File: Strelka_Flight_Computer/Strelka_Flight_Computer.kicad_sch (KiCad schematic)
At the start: 10 parts

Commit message: Started design for V2
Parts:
- removed R14, R15, R16, R17, R18, R19: 0, Resistor_SMD:R_0603_1608Metric_Pad0.98x0.95mm_HandSolder, symbol Device:R_Small
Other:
- removed sheet STM32F405
- added sheet STM32F407 (STM32F407.kicad_sch)
- sheet Actuators ports: added none; removed CONT_TEST_EN
- sheet Data_Interfaces ports: added CAN_RXD, CAN_TXD; removed SWCLK, SWDIO

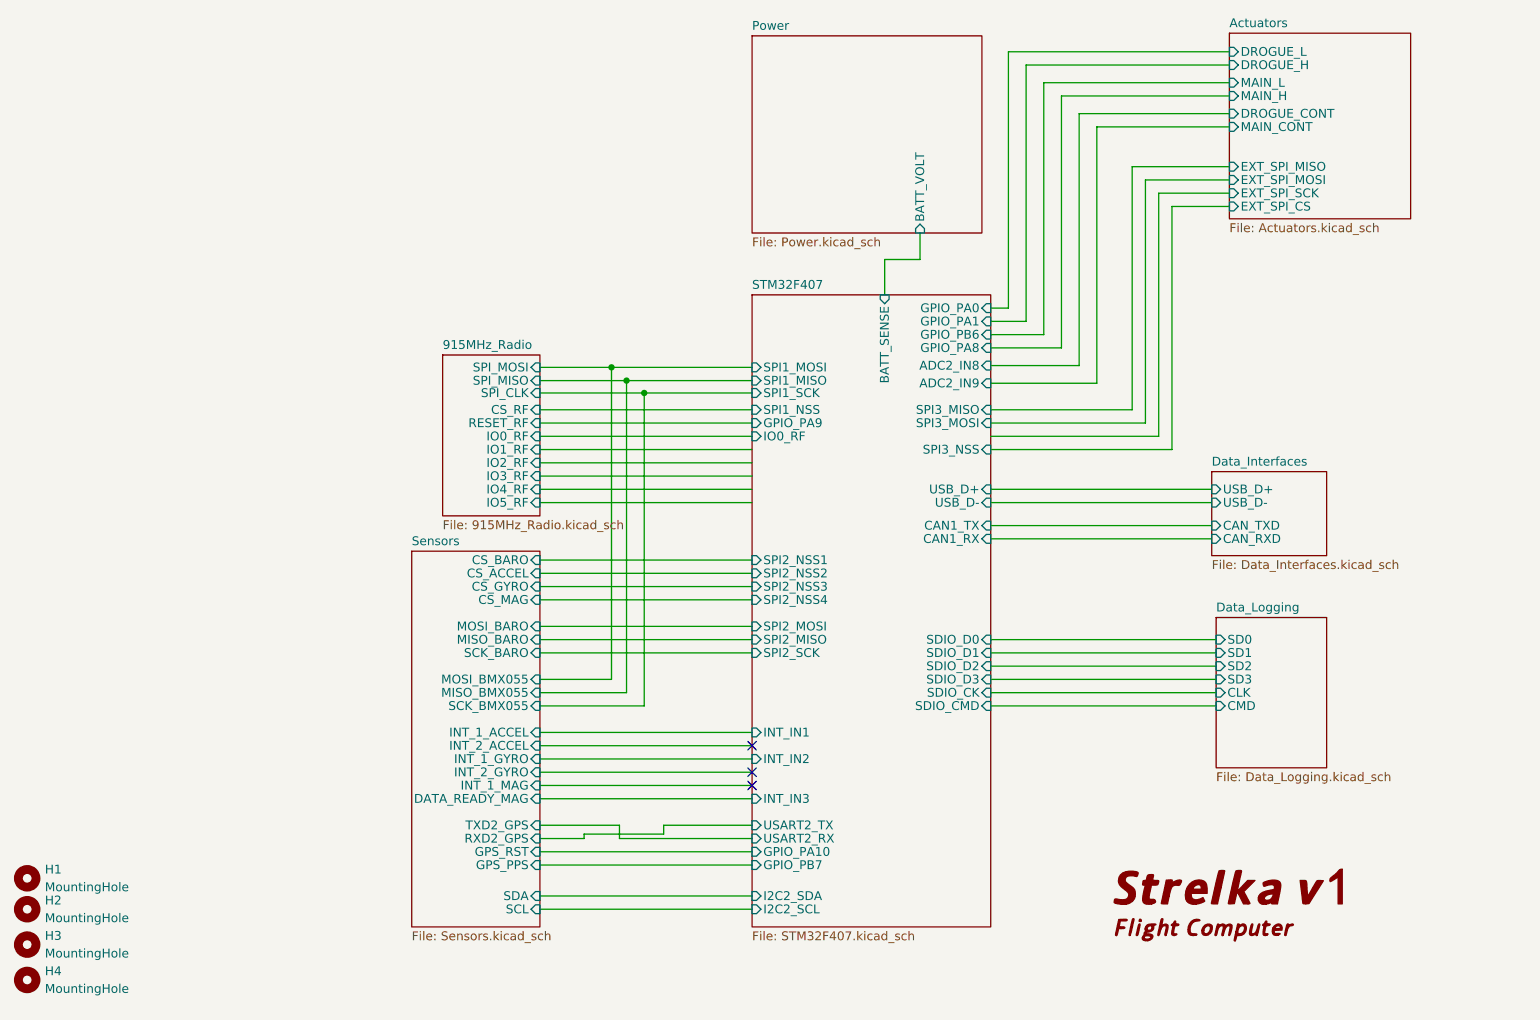
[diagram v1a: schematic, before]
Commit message: Changes main processor to h4745
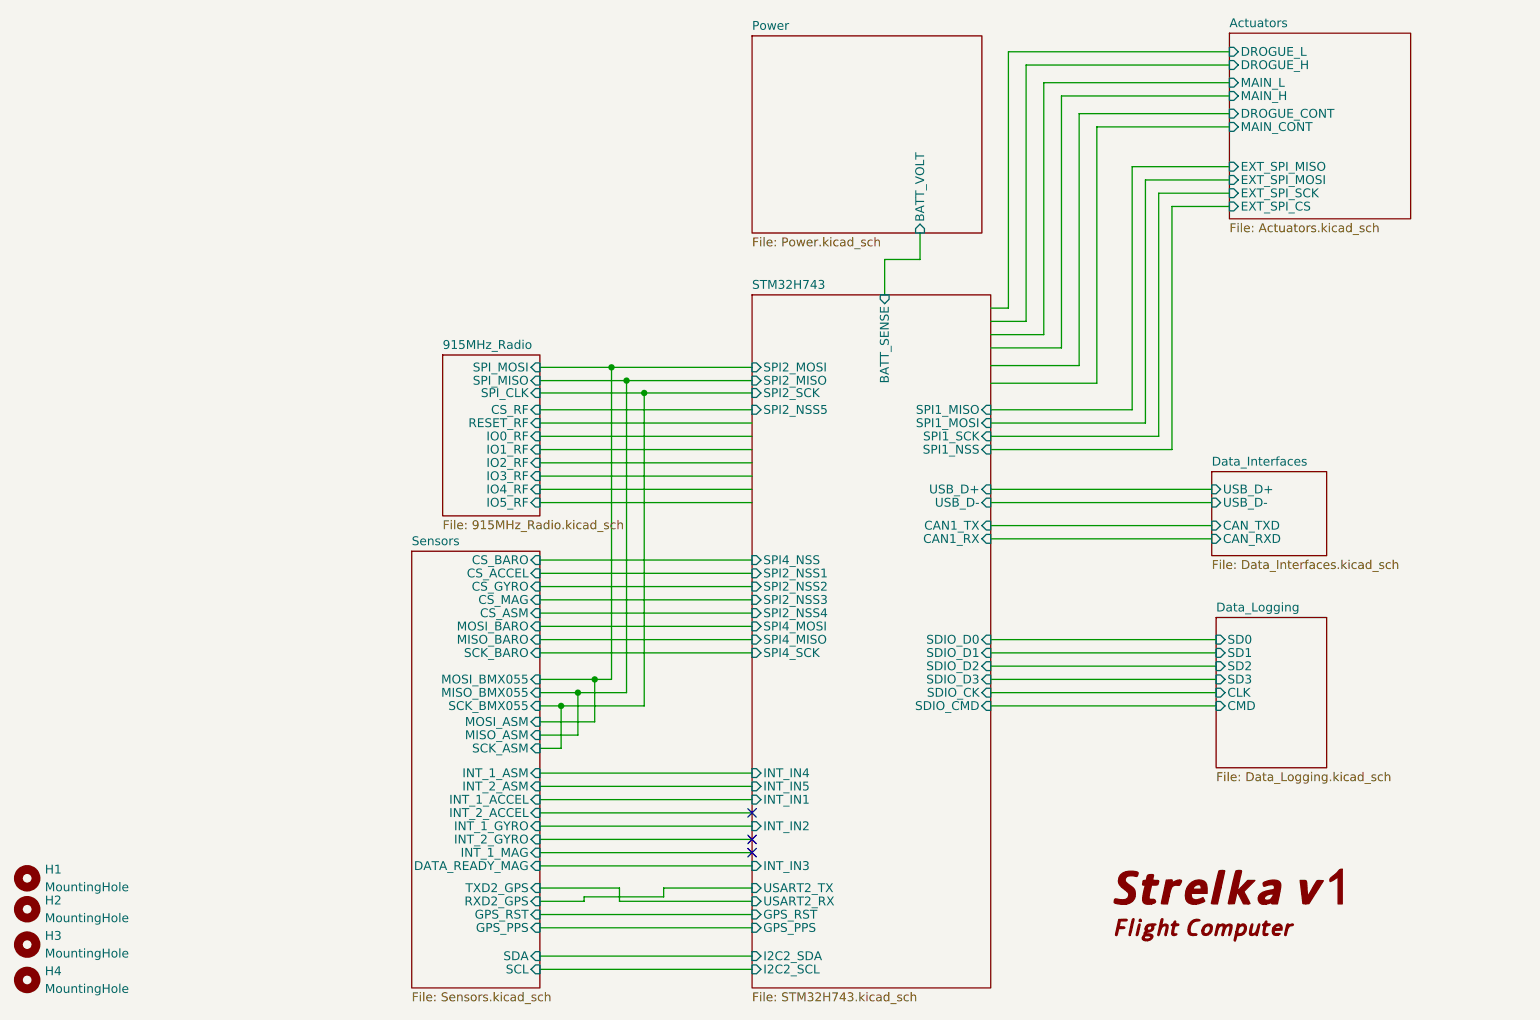
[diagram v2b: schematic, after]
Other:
- removed sheet STM32F407
- added sheet STM32H743 (STM32H743.kicad_sch)
- sheet Sensors ports: added CS_ASM, INT_1_ASM, INT_2_ASM, MISO_ASM, MOSI_ASM, SCK_ASM; removed none

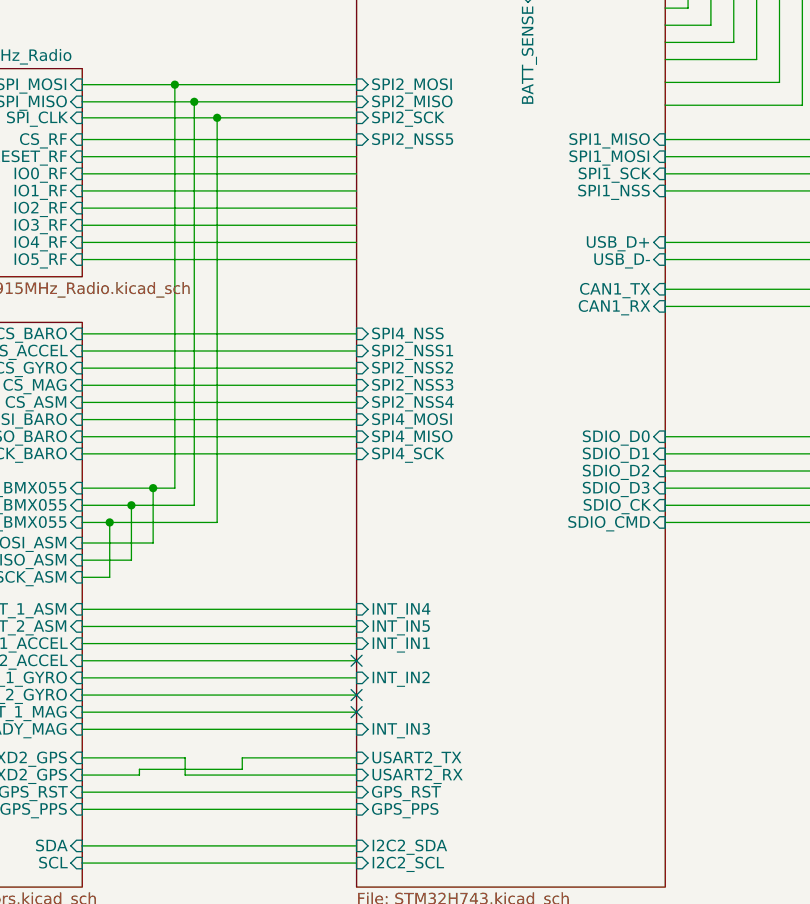
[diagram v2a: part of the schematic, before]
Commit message: Started component placement
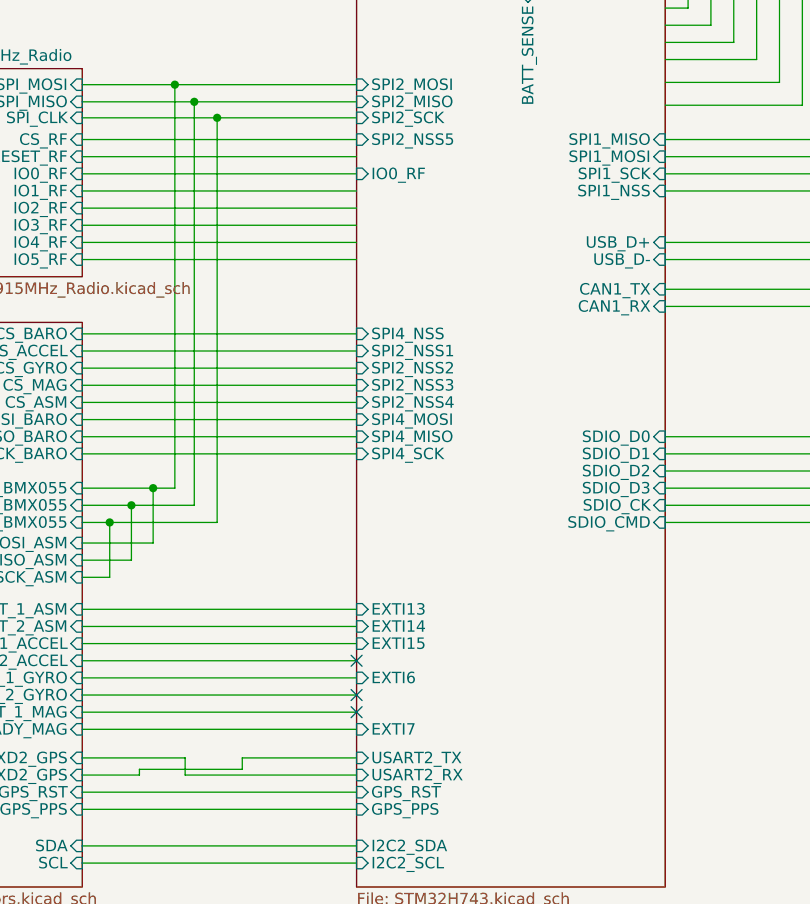
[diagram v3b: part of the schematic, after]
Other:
- sheet STM32H743 ports: added EXTI13, EXTI14, EXTI15, EXTI6, EXTI7, IO0_RF; removed INT_IN1, INT_IN2, INT_IN3, INT_IN4, INT_IN5
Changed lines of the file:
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@@
       (effects (font (size 1.27 1.27)) (justify right))
-    )
-    (pin "INT_IN1" input (at 127 158.877 180)
-      (effects (font (size 1.27 1.27)) (justify left))
     )
     (pin "SPI2_MISO" input (at 127 98.679 180)
@@
     (pin "SDIO_D1" input (at 161.29 137.795 0)
       (effects (font (size 1.27 1.27)) (justify right))
-    )
-    (pin "INT_IN3" input (at 127 168.402 180)
-      (effects (font (size 1.27 1.27)) (justify left))
-    )
-    (pin "INT_IN2" input (at 127 162.687 180)
-      (effects (font (size 1.27 1.27)) (justify left))
     )
     (pin "I2C2_SCL" input (at 127 183.261 180)
@@
       (effects (font (size 1.27 1.27)) (justify left))
     )
-    (pin "INT_IN4" input (at 127 155.067 180)
-      (effects (font (size 1.27 1.27)) (justify left))
-    )
-    (pin "INT_IN5" input (at 127 156.972 180)
-      (effects (font (size 1.27 1.27)) (justify left))
-    )
     (pin "GPS_PPS" input (at 127 177.292 180)
       (effects (font (size 1.27 1.27)) (justify left))
@@
       (effects (font (size 1.27 1.27)) (justify left))
     )
+    (pin "EXTI13" input (at 127 155.067 180)
+      (effects (font (size 1.27 1.27)) (justify left))
+    )
+    (pin "EXTI14" input (at 127 156.972 180)
+      (effects (font (size 1.27 1.27)) (justify left))
+    )
+    (pin "EXTI15" input (at 127 158.877 180)
+      (effects (font (size 1.27 1.27)) (justify left))
+    )
+    (pin "EXTI6" input (at 127 162.687 180)
+      (effects (font (size 1.27 1.27)) (justify left))
+    )
+    (pin "EXTI7" input (at 127 168.402 180)
+      (effects (font (size 1.27 1.27)) (justify left))
+    )
+    (pin "IO0_RF" input (at 127 106.68 180)
+      (effects (font (size 1.27 1.27)) (justify left))
+    )

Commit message: Routing complete
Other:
- sheet STM32H743 ports: added DROGUE_H, DROGUE_L, MAIN_H, MAIN_L; removed none
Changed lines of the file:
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@@
       (effects (font (size 1.27 1.27)) (justify left))
+    )
+    (pin "MAIN_L" input (at 161.29 92.075 0)
+      (effects (font (size 1.27 1.27)) (justify right))
+    )
+    (pin "MAIN_H" input (at 161.29 93.98 0)
+      (effects (font (size 1.27 1.27)) (justify right))
+    )
+    (pin "DROGUE_L" input (at 161.29 88.265 0)
+      (effects (font (size 1.27 1.27)) (justify right))
+    )
+    (pin "DROGUE_H" input (at 161.29 90.17 0)
+      (effects (font (size 1.27 1.27)) (justify right))
     )
     (instances

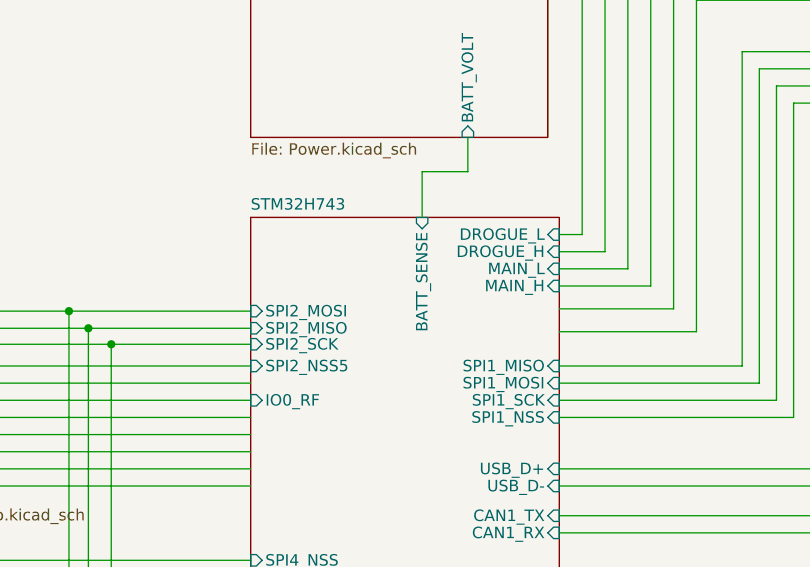
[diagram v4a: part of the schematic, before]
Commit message: Created BOM
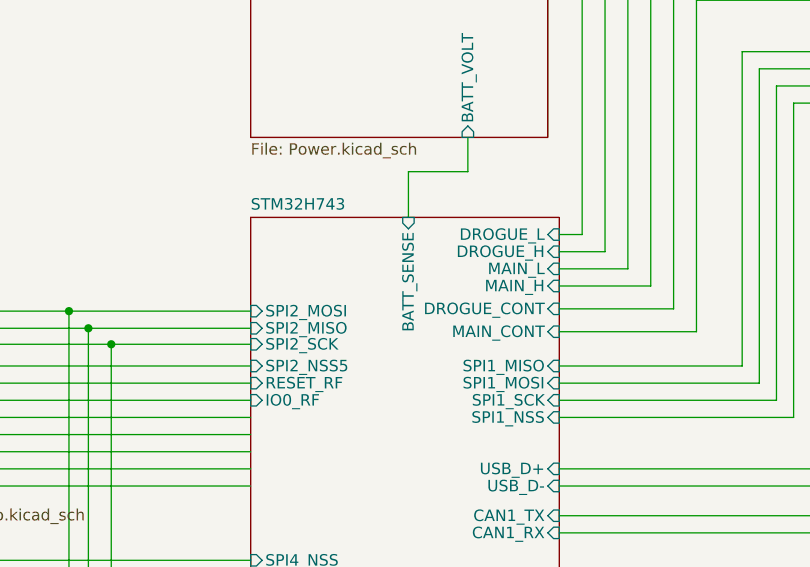
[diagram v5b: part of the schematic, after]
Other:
- sheet STM32H743 ports: added DROGUE_CONT, MAIN_CONT, RESET_RF; removed none
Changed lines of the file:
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@@
     (stroke (width 0) (type default))
   )
-  (wire (pts (xy 146.05 86.36) (xy 146.05 81.28))
+  (wire (pts (xy 144.526 86.36) (xy 144.526 81.28))
     (stroke (width 0) (type default))
   )
@@
     (stroke (width 0) (type default))
   )
-  (wire (pts (xy 146.05 81.28) (xy 151.13 81.28))
+  (wire (pts (xy 144.526 81.28) (xy 151.13 81.28))
     (stroke (width 0) (type default))
   )
@@
       (effects (font (size 1.27 1.27)) (justify left))
     )
-    (pin "BATT_SENSE" input (at 146.05 86.36 90)
+    (pin "BATT_SENSE" input (at 144.526 86.36 90)
       (effects (font (size 1.27 1.27)) (justify right))
     )
@@
       (effects (font (size 1.27 1.27)) (justify right))
     )
-    (instances
+    (pin "DROGUE_CONT" input (at 161.29 96.52 0)
+      (effects (font (size 1.27 1.27)) (justify right))
+    )
+    (pin "MAIN_CONT" input (at 161.29 99.06 0)
+      (effects (font (size 1.27 1.27)) (justify right))
+    )
+    (pin "RESET_RF" input (at 127 104.775 180)
+      (effects (font (size 1.27 1.27)) (justify left))
+    )
+    (instances

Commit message: Added LCSC mpn to all relevent parts
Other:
- sheet STM32H743 ports: added IO1_RF, IO2_RF; removed none
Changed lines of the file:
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@@
+      (effects (font (size 1.27 1.27)) (justify left))
+    )
+    (pin "IO1_RF" input (at 127 108.585 180)
+      (effects (font (size 1.27 1.27)) (justify left))
+    )
+    (pin "IO2_RF" input (at 127 110.49 180)
       (effects (font (size 1.27 1.27)) (justify left))
     )

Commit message: Adj to BOM
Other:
- note added: "Strelka V2 Flight Computer"
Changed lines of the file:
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@@
 (kicad_sch (version 20230121) (generator eeschema)
   (paper "A4")
+  (title_block
+    (rev "2")
+  )
   (junction (at 108.966 98.679) (diameter 0) (color 0 0 0 0)
   )
@@
   (wire (pts (xy 106.807 96.774) (xy 127 96.774))
     (stroke (width 0) (type default))
+  )
+  (text "Strelka V2\nFlight Computer" (at 177.8 181.61 0)
+    (effects (font (face "Dubai") (size 4 4) italic) (justify left bottom))
   )
   (symbol (lib_id "Mechanical:MountingHole") (at 22.86 174.625 0) (unit 1)
@@
         )
       )
-    )
-  )
-  (symbol (lib_id "Strelka_Logo:LOGO") (at 195.58 173.355 0) (unit 1)
-    (in_bom yes) (on_board yes) (dnp no) (fields_autoplaced)
-    (property "Reference" "#G1" (at 195.58 166.986 0)
-      (effects (font (size 1.27 1.27)) hide)
-    )
-    (property "Value" "LOGO" (at 195.58 179.724 0)
-      (effects (font (size 1.27 1.27)) hide)
-    )
-    (property "Footprint" "Footprints:Strelka_Logo" (at 195.58 173.355 0)
-      (effects (font (size 1.27 1.27)) hide)
-    )
-    (property "Datasheet" "" (at 195.58 173.355 0)
-      (effects (font (size 1.27 1.27)) hide)
-    )
-    (instances
-      (project "Strelka_Flight_Computer"
-        (path "/e63e39d7-6ac0-4ffd-8aa3-1841a4541b55"
-          (reference "#G1") (unit 1)
-        )
-      )
